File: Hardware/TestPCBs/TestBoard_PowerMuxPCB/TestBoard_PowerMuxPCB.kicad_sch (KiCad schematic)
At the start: 56 parts, among them J1 575-4, J2 575-4, J3 575-4, J4 575-4, J5 575-4, J6 53307-2471, J7 575-4, J8 Conn_01x03, J9 Conn_01x02, Q1 SQJQ140E-T1_GE3, Q2 SQJQ140E-T1_GE3, Q3 SQJQ140E-T1_GE3, Q4 SQJQ140E-T1_GE3

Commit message: change testpoint footprint
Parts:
- TP1, TP10, TP11, TP12, TP13, TP14, TP15, TP16, TP17, TP18, TP19, TP2, TP3, TP4, TP5, TP6, TP7, TP8, TP9: footprint TestPoint:TestPoint_Loop_D3.80mm_Drill2.0mm -> TestPoint:TestPoint_Loop_D3.50mm_Drill1.4mm_Beaded
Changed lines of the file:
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@@
 			)
 		)
-		(property "Footprint" "TestPoint:TestPoint_Loop_D3.80mm_Drill2.0mm"
+		(property "Footprint" "TestPoint:TestPoint_Loop_D3.50mm_Drill1.4mm_Beaded"
 			(at 264.16 123.19 0)
 			(effects
@@
 			)
 		)
-		(property "Footprint" "TestPoint:TestPoint_Loop_D3.80mm_Drill2.0mm"
+		(property "Footprint" "TestPoint:TestPoint_Loop_D3.50mm_Drill1.4mm_Beaded"
 			(at 220.98 133.35 0)
 			(effects
@@
 			)
 		)
-		(property "Footprint" "TestPoint:TestPoint_Loop_D3.80mm_Drill2.0mm"
+		(property "Footprint" "TestPoint:TestPoint_Loop_D3.50mm_Drill1.4mm_Beaded"
 			(at 220.98 139.7 0)
 			(effects
@@
 			)
 		)
-		(property "Footprint" "TestPoint:TestPoint_Loop_D3.80mm_Drill2.0mm"
+		(property "Footprint" "TestPoint:TestPoint_Loop_D3.50mm_Drill1.4mm_Beaded"
 			(at 220.98 115.57 0)
 			(effects
@@
 			)
 		)
-		(property "Footprint" "TestPoint:TestPoint_Loop_D3.80mm_Drill2.0mm"
+		(property "Footprint" "TestPoint:TestPoint_Loop_D3.50mm_Drill1.4mm_Beaded"
 			(at 220.98 123.19 0)
 			(effects
@@
 			)
 		)
-		(property "Footprint" "TestPoint:TestPoint_Loop_D3.80mm_Drill2.0mm"
+		(property "Footprint" "TestPoint:TestPoint_Loop_D3.50mm_Drill1.4mm_Beaded"
 			(at 241.3 115.57 0)
 			(effects
@@
 			)
 		)
-		(property "Footprint" "TestPoint:TestPoint_Loop_D3.80mm_Drill2.0mm"
+		(property "Footprint" "TestPoint:TestPoint_Loop_D3.50mm_Drill1.4mm_Beaded"
 			(at 201.93 115.57 0)
 			(effects
@@
 			)
 		)
-		(property "Footprint" "TestPoint:TestPoint_Loop_D3.80mm_Drill2.0mm"
+		(property "Footprint" "TestPoint:TestPoint_Loop_D3.50mm_Drill1.4mm_Beaded"
 			(at 201.93 139.7 0)
 			(effects
@@
 			)
 		)
-		(property "Footprint" "TestPoint:TestPoint_Loop_D3.80mm_Drill2.0mm"
+		(property "Footprint" "TestPoint:TestPoint_Loop_D3.50mm_Drill1.4mm_Beaded"
 			(at 201.93 123.19 0)
 			(effects
@@
 			)
 		)
-		(property "Footprint" "TestPoint:TestPoint_Loop_D3.80mm_Drill2.0mm"
+		(property "Footprint" "TestPoint:TestPoint_Loop_D3.50mm_Drill1.4mm_Beaded"
 			(at 241.3 139.7 0)
 			(effects
@@
 			)
 		)
-		(property "Footprint" "TestPoint:TestPoint_Loop_D3.80mm_Drill2.0mm"
+		(property "Footprint" "TestPoint:TestPoint_Loop_D3.50mm_Drill1.4mm_Beaded"
 			(at 201.93 133.35 0)
 			(effects
@@
 			)
 		)
-		(property "Footprint" "TestPoint:TestPoint_Loop_D3.80mm_Drill2.0mm"
+		(property "Footprint" "TestPoint:TestPoint_Loop_D3.50mm_Drill1.4mm_Beaded"
 			(at 264.16 115.57 0)
 			(effects
@@
 			)
 		)
-		(property "Footprint" "TestPoint:TestPoint_Loop_D3.80mm_Drill2.0mm"
+		(property "Footprint" "TestPoint:TestPoint_Loop_D3.50mm_Drill1.4mm_Beaded"
 			(at 205.74 25.4 0)
 			(effects
@@
 			)
 		)
-		(property "Footprint" "TestPoint:TestPoint_Loop_D3.80mm_Drill2.0mm"
+		(property "Footprint" "TestPoint:TestPoint_Loop_D3.50mm_Drill1.4mm_Beaded"
 			(at 241.3 133.35 0)
 			(effects
@@
 			)
 		)
-		(property "Footprint" "TestPoint:TestPoint_Loop_D3.80mm_Drill2.0mm"
+		(property "Footprint" "TestPoint:TestPoint_Loop_D3.50mm_Drill1.4mm_Beaded"
 			(at 143.51 72.39 0)
 			(effects
@@
 			)
 		)
-		(property "Footprint" "TestPoint:TestPoint_Loop_D3.80mm_Drill2.0mm"
+		(property "Footprint" "TestPoint:TestPoint_Loop_D3.50mm_Drill1.4mm_Beaded"
 			(at 76.2 25.4 0)
 			(effects
@@
 			)
 		)
-		(property "Footprint" "TestPoint:TestPoint_Loop_D3.80mm_Drill2.0mm"
+		(property "Footprint" "TestPoint:TestPoint_Loop_D3.50mm_Drill1.4mm_Beaded"
 			(at 264.16 139.7 0)
 			(effects
@@
 			)
 		)
-		(property "Footprint" "TestPoint:TestPoint_Loop_D3.80mm_Drill2.0mm"
+		(property "Footprint" "TestPoint:TestPoint_Loop_D3.50mm_Drill1.4mm_Beaded"
 			(at 241.3 123.19 0)
 			(effects
@@
 			)
 		)
-		(property "Footprint" "TestPoint:TestPoint_Loop_D3.80mm_Drill2.0mm"
+		(property "Footprint" "TestPoint:TestPoint_Loop_D3.50mm_Drill1.4mm_Beaded"
 			(at 264.16 132.08 0)
 			(effects

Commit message: test board mostly done
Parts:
- removed TP10, TP11, TP9: TestPoint, TestPoint:TestPoint_Loop_D3.50mm_Drill1.4mm_Beaded, symbol Connector:TestPoint
- J6: footprint UTSVT_Connectors:533072471 -> PowerBoardLib:LVMux
- J8: footprint Connector_PinSocket_2.54mm:PinSocket_1x03_P2.54mm_Vertical -> Connector_PinHeader_2.54mm:PinHeader_1x03_P2.54mm_Vertical
- R5, R6: footprint LV Carrier Library:RESC6432X89N -> PowerBoardLib:RESC6432X89N
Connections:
- net FTL1: no longer J6.7
- net FTL2: now also J6.7
- net GND: now also J9.1 (Pin_1); no longer J9.2 (Pin_2)
- net Out: now also J9.2 (Pin_2); no longer J9.1 (Pin_1)
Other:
- moved on the sheet: J9, TP12

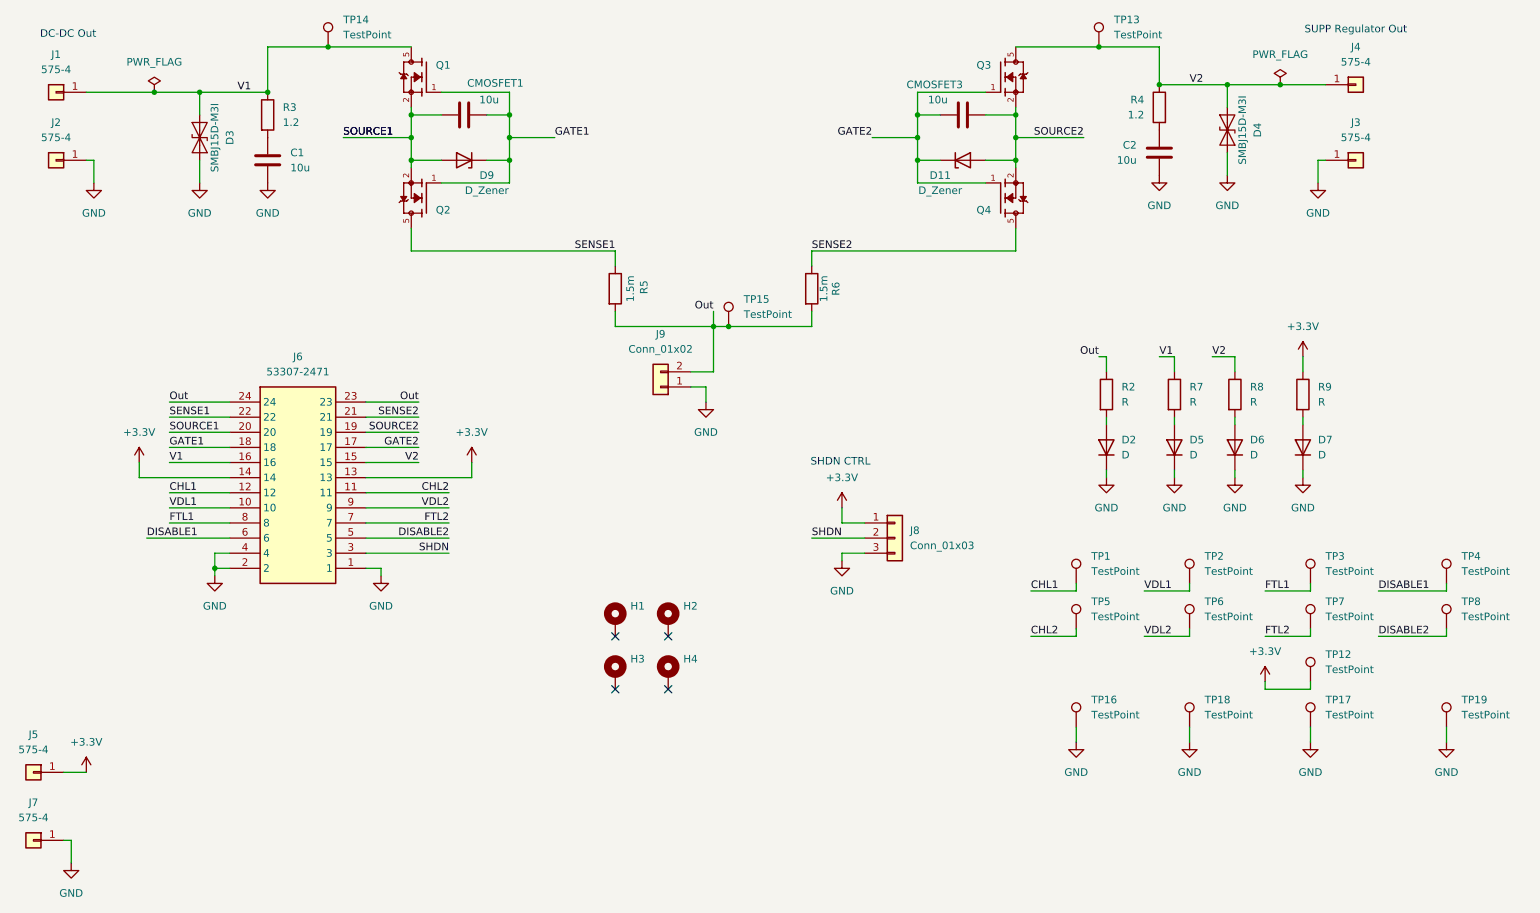
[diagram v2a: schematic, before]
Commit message: mux test board bom (#10)
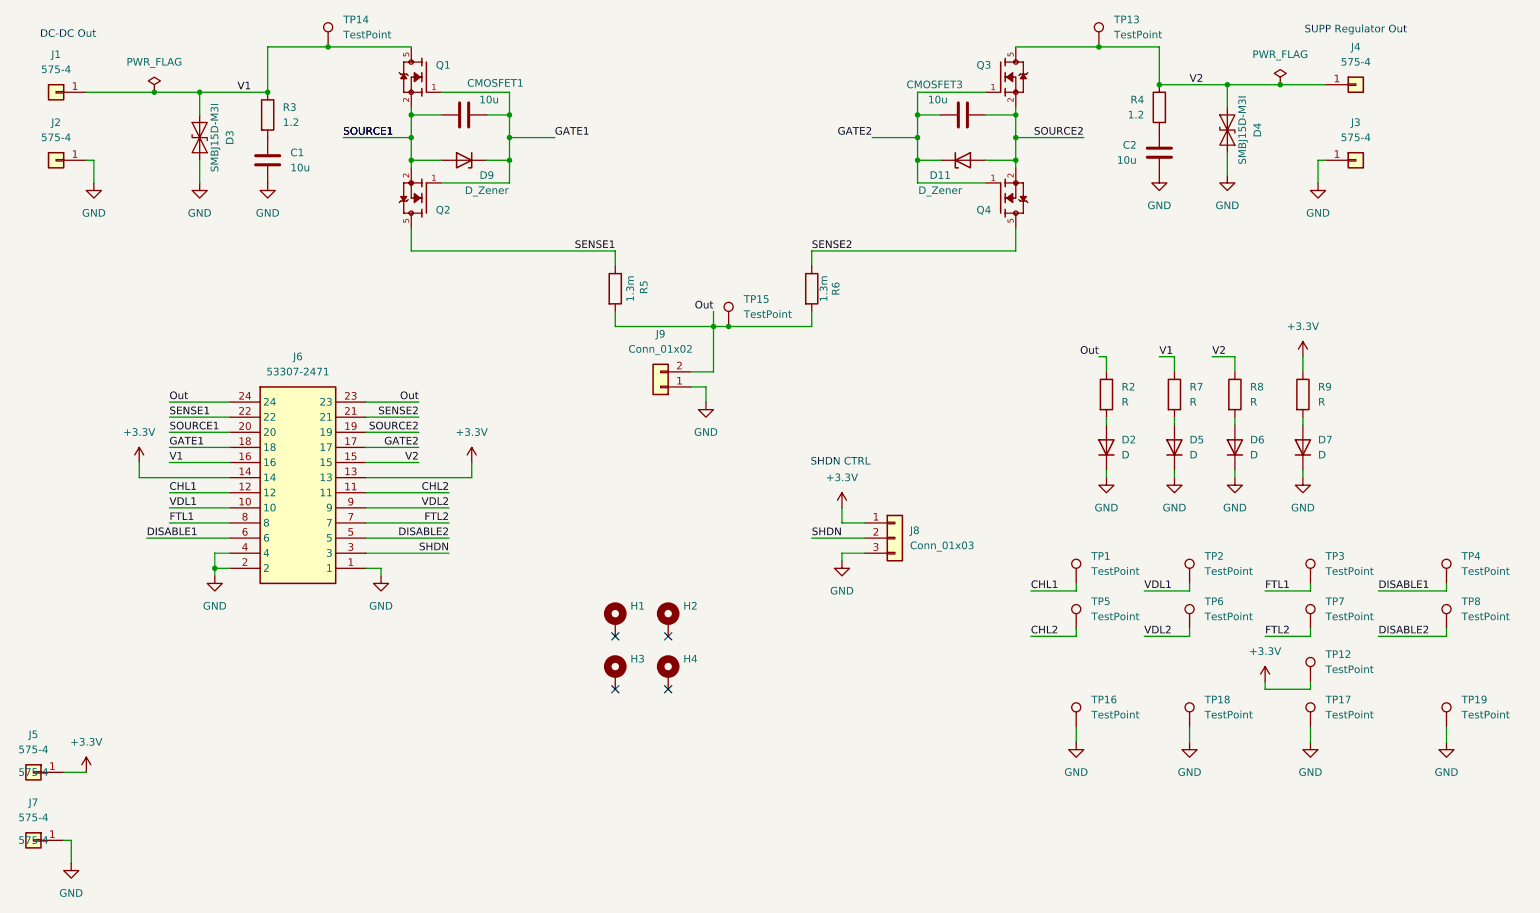
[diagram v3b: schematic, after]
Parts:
- C1, C2, CMOSFET1, CMOSFET3: P/N (none) -> TMK212BBJ106MGHT
- D11, D9: P/N (none) -> DDZ9703T-7
- D2, D5, D6, D7: P/N (none) -> LTST-C193TBKT-5A
- D3, D4: P/N (none) -> SMBJ33D
- J1, J2, J3, J4, J5, J7: P/N (none) -> 575-4
- J8, TP1, TP12, TP13, TP14, TP15, TP16, TP17, TP18, TP19, TP2, TP3, TP4, TP5, TP6, TP7, TP8: now left out of the parts list
- J9: P/N (none) -> PRT-10474
- Q1, Q2, Q3, Q4: P/N (none) -> SQJQ140E-T1_GE3
- R2, R7, R8, R9: P/N (none) -> CRCW06032K00FKEA
- R3, R4: MFG PN RK73H2ATTD1R20F -> CRCW06031R20FKEA; P/N (none) -> CRCW06031R20FKEA
- R5, R6: value 1.5m -> 1.3m; P/N (none) -> WSLF25121L300FEA

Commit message: fix basePCB libs
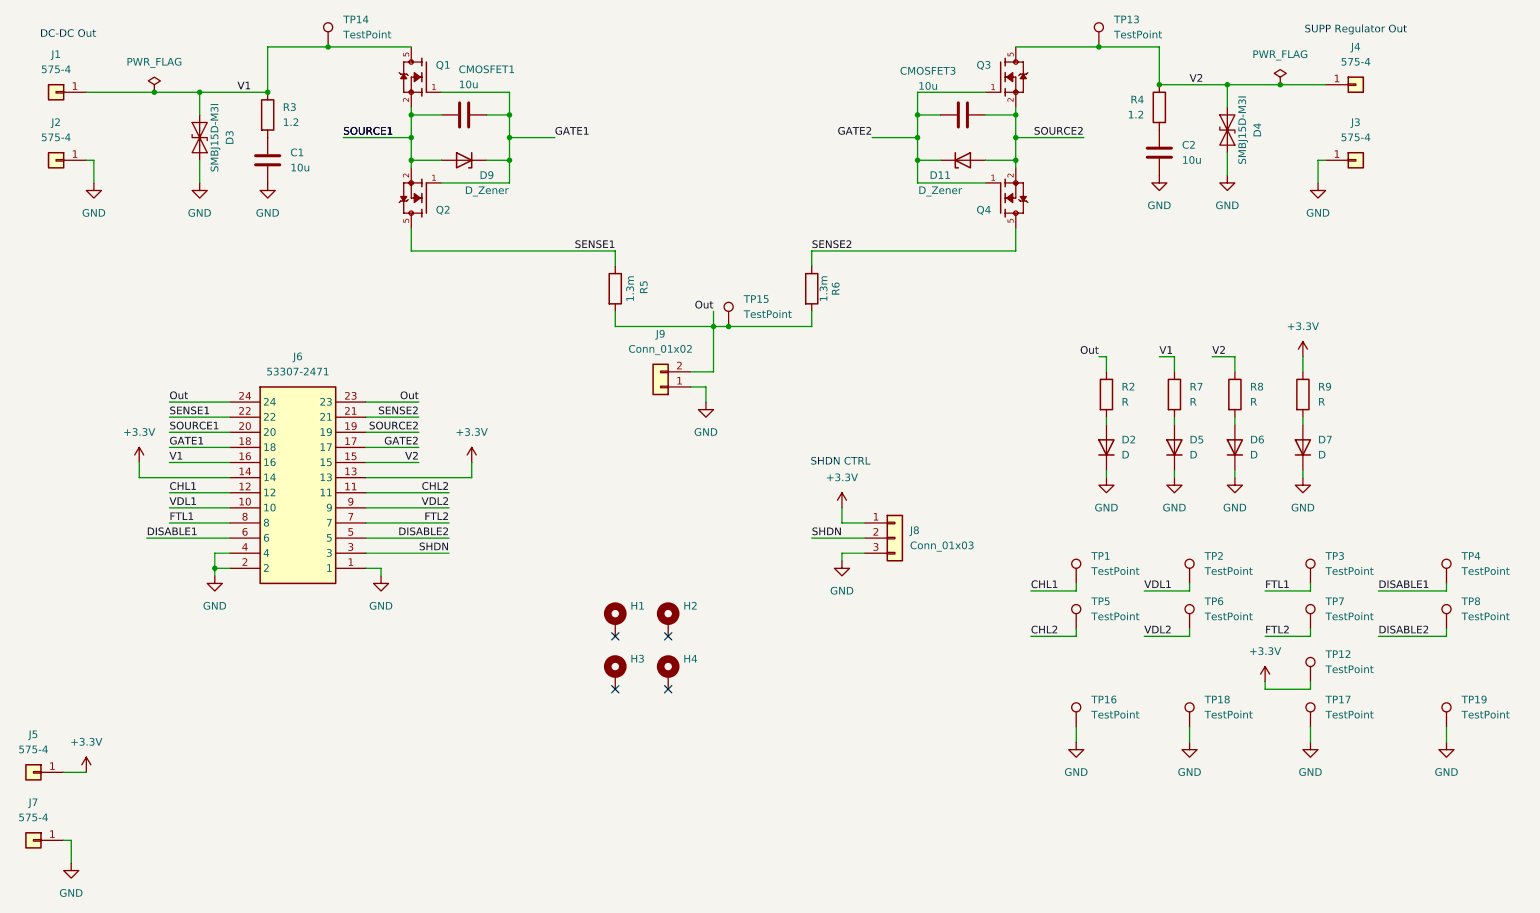
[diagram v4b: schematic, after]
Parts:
- removed C1, C2, CMOSFET1, CMOSFET3: 10u, Capacitor_SMD:C_0805_2012Metric, symbol ECE319K:C
- added C1, C2, CMOSFET1, CMOSFET3: 10u, Capacitor_SMD:C_0805_2012Metric, symbol Device:C
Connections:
- net GATE1: now also CMOSFET1.2
- net GATE2: now also CMOSFET3.2
- net GND: now also C1.2, C2.2
- net SOURCE1: now also CMOSFET1.1
- net SOURCE2: now also CMOSFET3.1
- net at R4.2: now also C2.1
- net at R3.2: now also C1.1

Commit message: stuff
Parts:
- D3, D4: footprint PowerBoardLib:P26_DO-214AA_SMB -> LV Carrier Library:SMBJ15DM3; symbol PowerBoardLib:SMBJ15D-M3I -> LV-Carrier:SMBJ15D-M3I; P/N SMBJ33D -> SMBJ15D-M3/I
- Q1, Q2, Q3, Q4: footprint PowerBoardLib:TO200P800X182-5N -> LV Carrier Library:SQJQ140E-T1_GE3; symbol PowerBoardLib:SQJQ140E-T1_GE3 -> LV-Carrier:SQJQ140E-T1_GE3
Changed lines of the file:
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@@
 	)
 	(symbol
-		(lib_id "PowerBoardLib:SQJQ140E-T1_GE3")
+		(lib_id "LV-Carrier:SQJQ140E-T1_GE3")
 		(at 184.15 30.48 0)
 		(unit 1)
@@
 			)
 		)
-		(property "Footprint" "PowerBoardLib:TO200P800X182-5N"
+		(property "Footprint" "LV Carrier Library:SQJQ140E-T1_GE3"
 			(at 184.15 30.48 0)
 			(effects
@@
 					(size 1.27 1.27)
 				)
+				(justify bottom)
 				(hide yes)
 			)
@@
 	)
 	(symbol
-		(lib_id "PowerBoardLib:SQJQ140E-T1_GE3")
+		(lib_id "LV-Carrier:SQJQ140E-T1_GE3")
 		(at 184.15 50.8 0)
 		(mirror x)
@@
 			)
 		)
-		(property "Footprint" "PowerBoardLib:TO200P800X182-5N"
+		(property "Footprint" "LV Carrier Library:SQJQ140E-T1_GE3"
 			(at 184.15 50.8 0)
 			(effects
@@
 					(size 1.27 1.27)
 				)
+				(justify bottom)
 				(hide yes)
 			)
@@
 	)
 	(symbol
-		(lib_id "PowerBoardLib:SQJQ140E-T1_GE3")
+		(lib_id "LV-Carrier:SQJQ140E-T1_GE3")
 		(at 87.63 50.8 180)
 		(unit 1)
@@
 			)
 		)
-		(property "Footprint" "PowerBoardLib:TO200P800X182-5N"
+		(property "Footprint" "LV Carrier Library:SQJQ140E-T1_GE3"
 			(at 87.63 50.8 0)
 			(effects
@@
 					(size 1.27 1.27)
 				)
+				(justify bottom)
 				(hide yes)
 			)
@@
 	)
 	(symbol
-		(lib_id "PowerBoardLib:SMBJ15D-M3I")
+		(lib_id "LV-Carrier:SMBJ15D-M3I")
 		(at 222.25 39.37 270)
 		(unit 1)
@@
 			)
 		)
-		(property "Footprint" "PowerBoardLib:P26_DO-214AA_SMB"
+		(property "Footprint" "LV Carrier Library:SMBJ15DM3"
 			(at 219.71 39.37 0)
 			(effects
@@
 			)
 		)
-		(property "P/N" "SMBJ33D"
+		(property "P/N" "SMBJ15D-M3/I "
 			(at 222.25 39.37 0)
 			(effects
@@
 	)
 	(symbol
-		(lib_id "PowerBoardLib:SMBJ15D-M3I")
+		(lib_id "LV-Carrier:SMBJ15D-M3I")
 		(at 49.53 40.64 270)
 		(unit 1)
@@
 			)
 		)
-		(property "Footprint" "PowerBoardLib:P26_DO-214AA_SMB"
+		(property "Footprint" "LV Carrier Library:SMBJ15DM3"
 			(at 46.99 40.64 0)
 			(effects
@@
 			)
 		)
-		(property "P/N" "SMBJ33D"
+		(property "P/N" "SMBJ15D-M3/I "
 			(at 49.53 40.64 0)
 			(effects
@@
 	)
 	(symbol
-		(lib_id "PowerBoardLib:SQJQ140E-T1_GE3")
+		(lib_id "LV-Carrier:SQJQ140E-T1_GE3")
 		(at 87.63 30.48 0)
 		(mirror y)
@@
 			)
 		)
-		(property "Footprint" "PowerBoardLib:TO200P800X182-5N"
+		(property "Footprint" "LV Carrier Library:SQJQ140E-T1_GE3"
 			(at 87.63 30.48 0)
 			(effects
@@
 					(size 1.27 1.27)
 				)
+				(justify bottom)
 				(hide yes)
 			)

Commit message: lv mux test board
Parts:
- added J10, J11: Conn_01x02, Connector_PinHeader_2.54mm:PinHeader_1x02_P2.54mm_Vertical, symbol Connector_Generic:Conn_01x02
- J6: footprint PowerBoardLib:LVMux -> LV Carrier Library:LVMux
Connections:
- net GATE1: now also J10.1 (Pin_1)
- net GATE2: now also J11.1 (Pin_1)
- net SOURCE1: now also J10.2 (Pin_2)
- net SOURCE2: now also J11.2 (Pin_2)
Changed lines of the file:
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@@
 	(wire
 		(pts
+			(xy 105.41 26.67) (xy 115.57 26.67)
+		)
+		(stroke
+			(width 0)
+			(type default)
+		)
+	)
+	(wire
+		(pts
 			(xy 30.48 44.45) (xy 31.75 44.45)
 		)
@@
 	(wire
 		(pts
+			(xy 139.7 24.13) (xy 147.32 24.13)
+		)
+		(stroke
+			(width 0)
+			(type default)
+		)
+	)
+	(wire
+		(pts
 			(xy 162.56 40.64) (xy 170.18 40.64)
 		)
@@
 	(wire
 		(pts
+			(xy 105.41 24.13) (xy 115.57 24.13)
+		)
+		(stroke
+			(width 0)
+			(type default)
+		)
+	)
+	(wire
+		(pts
 			(xy 231.14 31.75) (xy 238.76 31.75)
 		)
@@
 	(wire
 		(pts
+			(xy 138.43 26.67) (xy 147.32 26.67)
+		)
+		(stroke
+			(width 0)
+			(type default)
+		)
+	)
+	(wire
+		(pts
 			(xy 157.48 110.49) (xy 161.29 110.49)
 		)
@@
 		)
 	)
+	(label "SOURCE2"
+		(at 138.43 26.67 0)
+		(effects
+			(font
+				(size 1.27 1.27)
+			)
+			(justify left bottom)
+		)
+	)
 	(label "GATE2"
 		(at 86.36 92.71 180)
@@
 		)
 	)
+	(label "GATE1"
+		(at 105.41 24.13 0)
+		(effects
+			(font
+				(size 1.27 1.27)
+			)
+			(justify left bottom)
+		)
+	)
 	(label "SHDN"
 		(at 91.44 110.49 180)
@@
 		)
 	)
+	(label "SOURCE1"
+		(at 105.41 26.67 0)
+		(effects
+			(font
+				(size 1.27 1.27)
+			)
+			(justify left bottom)
+		)
+	)
 	(label "FTL1"
 		(at 44.45 105.41 0)
@@
 		)
 	)
+	(label "GATE2"
+		(at 139.7 24.13 0)
+		(effects
+			(font
+				(size 1.27 1.27)
+			)
+			(justify left bottom)
+		)
+	)
 	(label "Out"
 		(at 44.45 85.09 0)
@@
 	)
 	(symbol
+		(lib_id "Connector_Generic:Conn_01x02")
+		(at 152.4 24.13 0)
+		(unit 1)
+		(exclude_from_sim no)
+		(in_bom yes)
+		(on_board yes)
+		(dnp no)
+		(fields_autoplaced yes)
+		(property "Reference" "J11"
+			(at 154.94 24.1299 0)
+			(effects
+				(font
+					(size 1.27 1.27)
+				)
+				(justify left)
+			)
+		)
+		(property "Value" "Conn_01x02"
+			(at 154.94 26.6699 0)
+			(effects
+				(font
+					(size 1.27 1.27)
+				)
+				(justify left)
+			)
+		)
+		(property "Footprint" "Connector_PinHeader_2.54mm:PinHeader_1x02_P2.54mm_Vertical"
+			(at 152.4 24.13 0)
+			(effects
+				(font
+					(size 1.27 1.27)
+				)
+				(hide yes)
+			)
+		)
+		(property "Datasheet" "~"
+			(at 152.4 24.13 0)
+			(effects
+				(font
+					(size 1.27 1.27)
+				)
+				(hide yes)
+			)
+		)
+		(property "Description" "Generic connector, single row, 01x02, script generated (kicad-library-utils/schlib/autogen/connector/)"
+			(at 152.4 24.13 0)
+			(effects
+				(font
+					(size 1.27 1.27)
+				)
+				(hide yes)
+			)
+		)
+		(pin "2"
+		)
+		(pin "1"
+		)
+		(instances
+			(project "TestBoard_PowerMuxPCB"
+				(path "/d2a44f9f-e32d-4fda-842e-1df06561b52d"
+					(reference "J11")
+					(unit 1)
+				)
+			)
+		)
+	)
+	(symbol
 		(lib_id "Device:D")
 		(at 234.95 92.71 90)
@@
 	)
 	(symbol
+		(lib_id "Connector_Generic:Conn_01x02")
+		(at 120.65 24.13 0)
+		(unit 1)
+		(exclude_from_sim no)
+		(in_bom yes)
+		(on_board yes)
+		(dnp no)
+		(fields_autoplaced yes)
+		(property "Reference" "J10"
+			(at 123.19 24.1299 0)
+			(effects
+				(font
+					(size 1.27 1.27)
+				)
+				(justify left)
+			)
+		)
+		(property "Value" "Conn_01x02"
+			(at 123.19 26.6699 0)
+			(effects
+				(font
+					(size 1.27 1.27)
+				)
+				(justify left)
+			)
+		)
+		(property "Footprint" "Connector_PinHeader_2.54mm:PinHeader_1x02_P2.54mm_Vertical"
+			(at 120.65 24.13 0)
+			(effects
+				(font
+					(size 1.27 1.27)
+				)
+				(hide yes)
+			)
+		)
+		(property "Datasheet" "~"
+			(at 120.65 24.13 0)
+			(effects
+				(font
+					(size 1.27 1.27)
+				)
+				(hide yes)
+			)
+		)
+		(property "Description" "Generic connector, single row, 01x02, script generated (kicad-library-utils/schlib/autogen/connector/)"
+			(at 120.65 24.13 0)
+			(effects
+				(font
+					(size 1.27 1.27)
+				)
+				(hide yes)
+			)
+		)
+		(pin "2"
+		)
+		(pin "1"
+		)
+		(instances
+			(project ""
+				(path "/d2a44f9f-e32d-4fda-842e-1df06561b52d"
+					(reference "J10")
+					(unit 1)
+				)
+			)
+		)
+	)
+	(symbol
 		(lib_id "Device:D_Zener")
 		(at 177.8 44.45 0)
@@
 			)
 		)
-		(property "Footprint" "PowerBoardLib:LVMux"
+		(property "Footprint" "LV Carrier Library:LVMux"
 			(at 73.66 180.01 0)
 			(effects
